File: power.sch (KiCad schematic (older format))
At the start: 37 parts

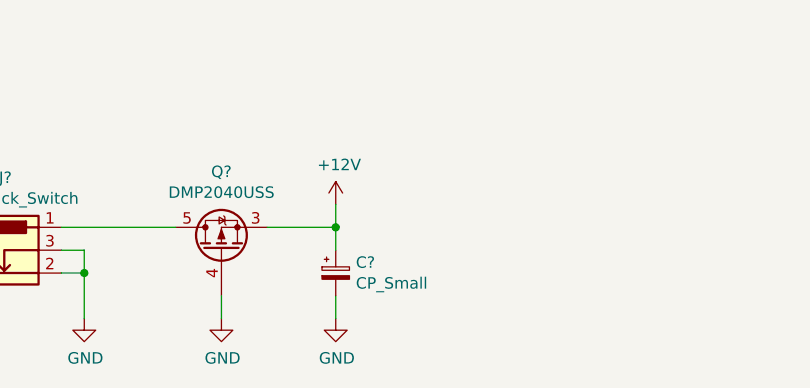
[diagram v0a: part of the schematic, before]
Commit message: sch: Set DC input cap value
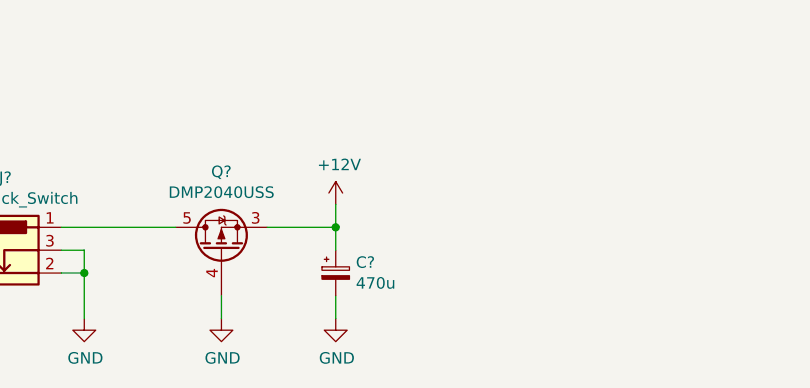
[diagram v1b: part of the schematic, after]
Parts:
- C?: value CP_Small -> 470u
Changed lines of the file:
@@
 P 4200 6900
 F 0 "C?" H 4288 6946 50  0000 L CNN
-F 1 "CP_Small" H 4288 6855 50  0000 L CNN
+F 1 "470u" H 4288 6855 50  0000 L CNN
 F 2 "" H 4200 6900 50  0001 C CNN
 F 3 "~" H 4200 6900 50  0001 C CNN

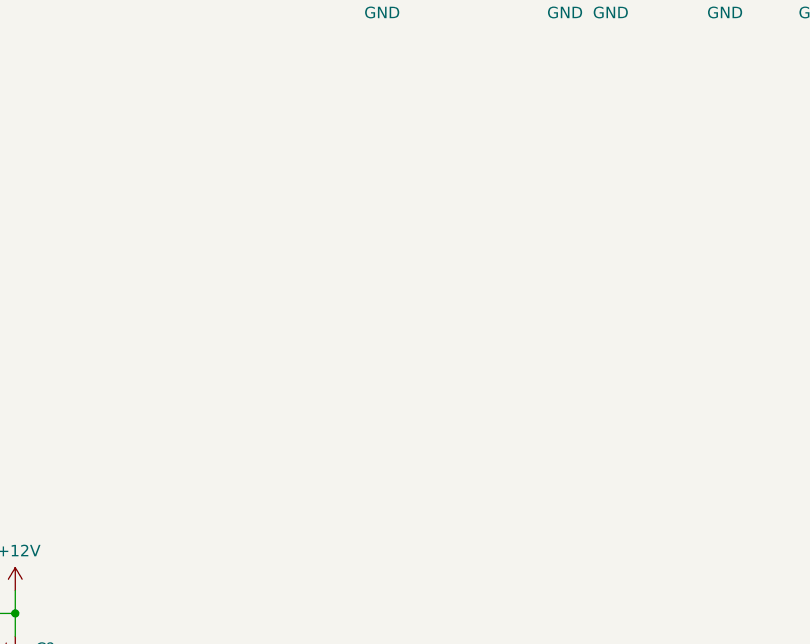
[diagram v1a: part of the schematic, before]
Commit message: sch, lib: Add 1V rail with TPS74401 LDO
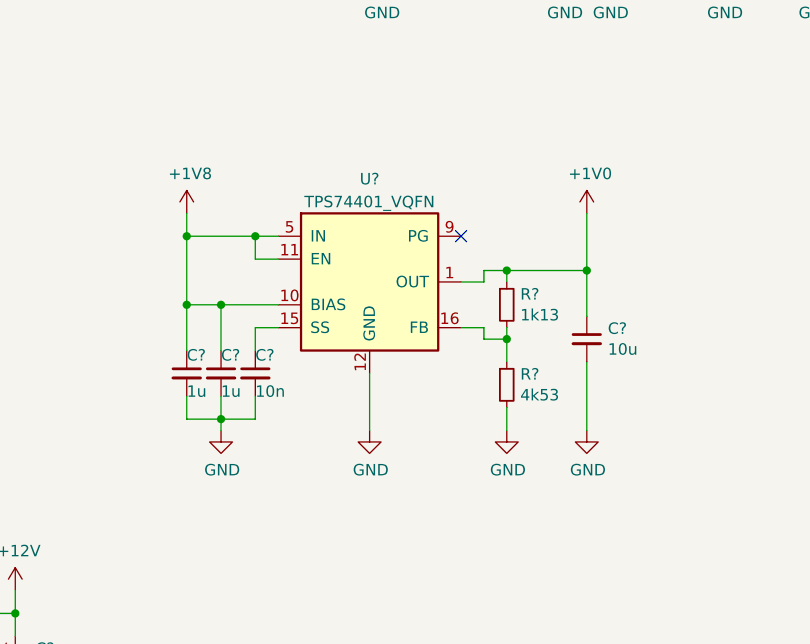
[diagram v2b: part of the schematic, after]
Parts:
- added C?: 10n, symbol Device:C_Small
- added C? (x2): 1u, symbol Device:C_Small
- added C?: 10u, symbol Device:C_Small
- added R?: 1k13, symbol Device:R_Small
- added R?: 4k53, symbol Device:R_Small
- added U?: TPS74401_VQFN, symbol pimouss-motherboard:TPS74401_VQFN
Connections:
- net labels added: +1V0, +1V8
- wire segments 191 -> 224
- no-connect marks 2 -> 3
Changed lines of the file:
@@
 Wire Wire Line
 	4200 7000 4200 7100
+$Comp
+L pimouss-motherboard:TPS74401_VQFN U?
+U 1 1 5CE43F9B
+P 5450 4950
+F 0 "U?" H 5750 5100 50  0000 C CNN
+F 1 "TPS74401_VQFN" H 5750 5000 50  0000 C CNN
+F 2 "" H 6250 4350 50  0001 C CNN
+F 3 "http://www.ti.com/general/docs/lit/getliterature.tsp?genericPartNumber=tps74401&fileType=pdf" H 5450 5450 50  0001 C CNN
+	1    5450 4950
+	1    0    0    -1
+$EndComp
+Wire Wire Line
+	5350 5150 5250 5150
+Wire Wire Line
+	5250 5150 5250 5050
+Wire Wire Line
+	5250 5050 5350 5050
+$Comp
+L Device:C_Small C?
+U 1 1 5CE5AE8A
+P 5250 5650
+F 0 "C?" H 5250 5700 50  0000 L BNN
+F 1 "10n" H 5250 5600 50  0000 L TNN
+F 2 "" H 5250 5650 50  0001 C CNN
+F 3 "~" H 5250 5650 50  0001 C CNN
+	1    5250 5650
+	1    0    0    -1
+$EndComp
+$Comp
+L Device:C_Small C?
+U 1 1 5CE5EC39
+P 5100 5650
+F 0 "C?" H 5100 5700 50  0000 L BNN
+F 1 "1u" H 5100 5600 50  0000 L TNN
+F 2 "" H 5100 5650 50  0001 C CNN
+F 3 "~" H 5100 5650 50  0001 C CNN
+	1    5100 5650
+	1    0    0    -1
+$EndComp
+$Comp
+L Device:C_Small C?
+U 1 1 5CE5F078
+P 4950 5650
+F 0 "C?" H 4950 5700 50  0000 L BNN
+F 1 "1u" H 4950 5600 50  0000 L TNN
+F 2 "" H 4950 5650 50  0001 C CNN
+F 3 "~" H 4950 5650 50  0001 C CNN
+	1    4950 5650
+	1    0    0    -1
+$EndComp
+Wire Wire Line
+	5250 5550 5250 5450
+Wire Wire Line
+	5250 5450 5350 5450
+Wire Wire Line
+	5100 5550 5100 5350
+Wire Wire Line
+	5100 5350 5350 5350
+Wire Wire Line
+	4950 5550 4950 5350
+Wire Wire Line
+	4950 5050 5250 5050
+Connection ~ 5250 5050
+Wire Wire Line
+	4950 5050 4950 4950
+Connection ~ 4950 5050
+$Comp
+L power:+1V8 #PWR?
+U 1 1 5CE8606F
+P 4950 4950
+F 0 "#PWR?" H 4950 4800 50  0001 C CNN
+F 1 "+1V8" H 4965 5123 50  0000 C CNN
+F 2 "" H 4950 4950 50  0001 C CNN
+F 3 "" H 4950 4950 50  0001 C CNN
+	1    4950 4950
+	1    0    0    -1
+$EndComp
+$Comp
+L power:GND #PWR?
+U 1 1 5CE86F6F
+P 5100 5900
+F 0 "#PWR?" H 5100 5650 50  0001 C CNN
+F 1 "GND" H 5105 5727 50  0000 C CNN
+F 2 "" H 5100 5900 50  0001 C CNN
+F 3 "" H 5100 5900 50  0001 C CNN
+	1    5100 5900
+	1    0    0    -1
+$EndComp
+Wire Wire Line
+	4950 5750 4950 5850
+Wire Wire Line
+	4950 5850 5100 5850
+Wire Wire Line
+	5250 5850 5250 5750
+Wire Wire Line
+	5100 5750 5100 5850
+Connection ~ 5100 5850
+Wire Wire Line
+	5100 5850 5250 5850
+Wire Wire Line
+	5100 5850 5100 5900
+$Comp
+L Device:R_Small R?
+U 1 1 5CEBCD64
+P 6350 5350
+F 0 "R?" H 6409 5396 50  0000 L CNN
+F 1 "1k13" H 6409 5305 50  0000 L CNN
+F 2 "" H 6350 5350 50  0001 C CNN
+F 3 "~" H 6350 5350 50  0001 C CNN
+	1    6350 5350
+	1    0    0    -1
+$EndComp
+$Comp
+L Device:R_Small R?
+U 1 1 5CED2DA2
+P 6350 5700
+F 0 "R?" H 6409 5746 50  0000 L CNN
+F 1 "4k53" H 6409 5655 50  0000 L CNN
+F 2 "" H 6350 5700 50  0001 C CNN
+F 3 "~" H 6350 5700 50  0001 C CNN
+	1    6350 5700
+	1    0    0    -1
+$EndComp
+$Comp
+L power:GND #PWR?
+U 1 1 5CED3182
+P 5750 5900
+F 0 "#PWR?" H 5750 5650 50  0001 C CNN
+F 1 "GND" H 5755 5727 50  0000 C CNN
+F 2 "" H 5750 5900 50  0001 C CNN
+F 3 "" H 5750 5900 50  0001 C CNN
+	1    5750 5900
+	1    0    0    -1
+$EndComp
+$Comp
+L power:GND #PWR?
+U 1 1 5CED54E7
+P 6350 5900
+F 0 "#PWR?" H 6350 5650 50  0001 C CNN
+F 1 "GND" H 6355 5727 50  0000 C CNN
+F 2 "" H 6350 5900 50  0001 C CNN
+F 3 "" H 6350 5900 50  0001 C CNN
+	1    6350 5900
+	1    0    0    -1
+$EndComp
+Wire Wire Line
+	6150 5450 6250 5450
+Wire Wire Line
+	6350 5800 6350 5900
+Wire Wire Line
+	5750 5650 5750 5900
+$Comp
+L power:+1V0 #PWR?
+U 1 1 5CF532E8
+P 6700 4950
+F 0 "#PWR?" H 6700 4800 50  0001 C CNN
+F 1 "+1V0" H 6715 5123 50  0000 C CNN
+F 2 "" H 6700 4950 50  0001 C CNN
+F 3 "" H 6700 4950 50  0001 C CNN
+	1    6700 4950
+	1    0    0    -1
+$EndComp
+$Comp
+L Device:C_Small C?
+U 1 1 5CF610D5
+P 6700 5500
+F 0 "C?" H 6792 5546 50  0000 L CNN
+F 1 "10u" H 6792 5455 50  0000 L CNN
+F 2 "" H 6700 5500 50  0001 C CNN
+F 3 "~" H 6700 5500 50  0001 C CNN
+	1    6700 5500
+	1    0    0    -1
+$EndComp
+Wire Wire Line
+	6700 5600 6700 5900
+$Comp
+L power:GND #PWR?
+U 1 1 5CF7AEEC
+P 6700 5900
+F 0 "#PWR?" H 6700 5650 50  0001 C CNN
+F 1 "GND" H 6705 5727 50  0000 C CNN
+F 2 "" H 6700 5900 50  0001 C CNN
+F 3 "" H 6700 5900 50  0001 C CNN
+	1    6700 5900
+	1    0    0    -1
+$EndComp
+Wire Wire Line
+	5100 5350 4950 5350
+Connection ~ 5100 5350
+Connection ~ 4950 5350
+Wire Wire Line
+	4950 5350 4950 5050
+NoConn ~ 6150 5050
+Wire Wire Line
+	6350 5450 6350 5500
+Wire Wire Line
+	6700 4950 6700 5200
+Wire Wire Line
+	6250 5450 6250 5500
+Wire Wire Line
+	6250 5500 6350 5500
+Connection ~ 6350 5500
+Wire Wire Line
+	6350 5500 6350 5600
+Wire Wire Line
+	6150 5250 6250 5250
+Wire Wire Line
+	6250 5250 6250 5200
+Wire Wire Line
+	6250 5200 6350 5200
+Wire Wire Line
+	6350 5200 6350 5250
+Wire Wire Line
+	6350 5200 6700 5200
+Connection ~ 6350 5200
+Connection ~ 6700 5200
+Wire Wire Line
+	6700 5200 6700 5400
 $EndSCHEMATC

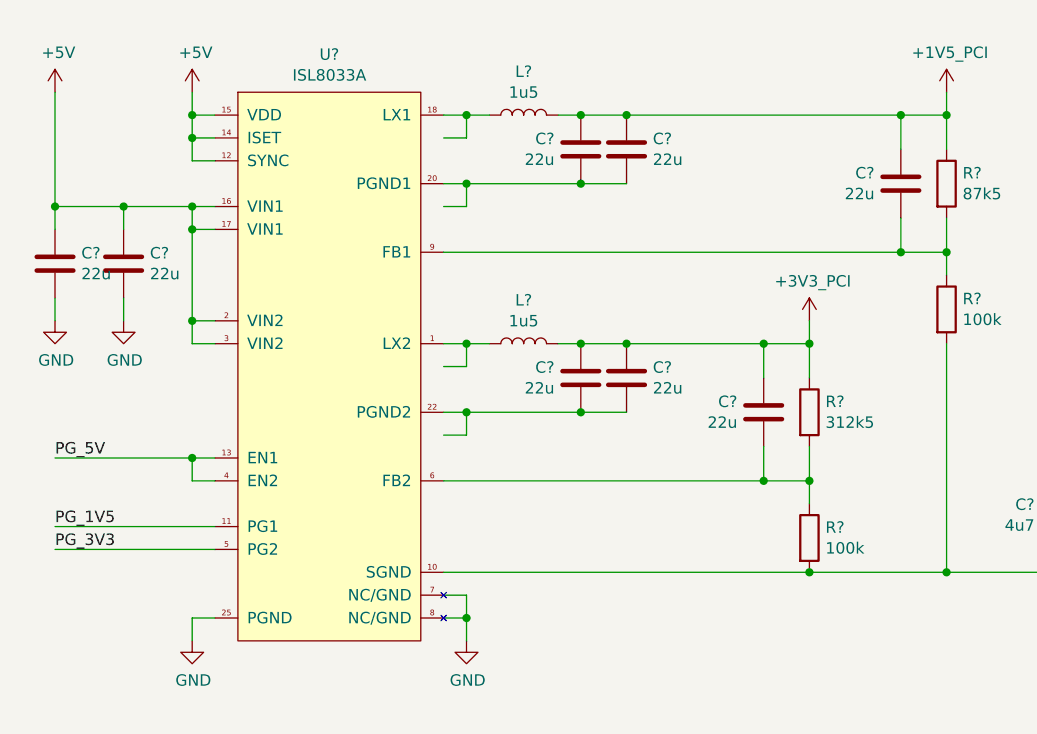
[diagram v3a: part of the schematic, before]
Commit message: sch: Replace regular symbols with small variant
Done for most capacitors and resistors
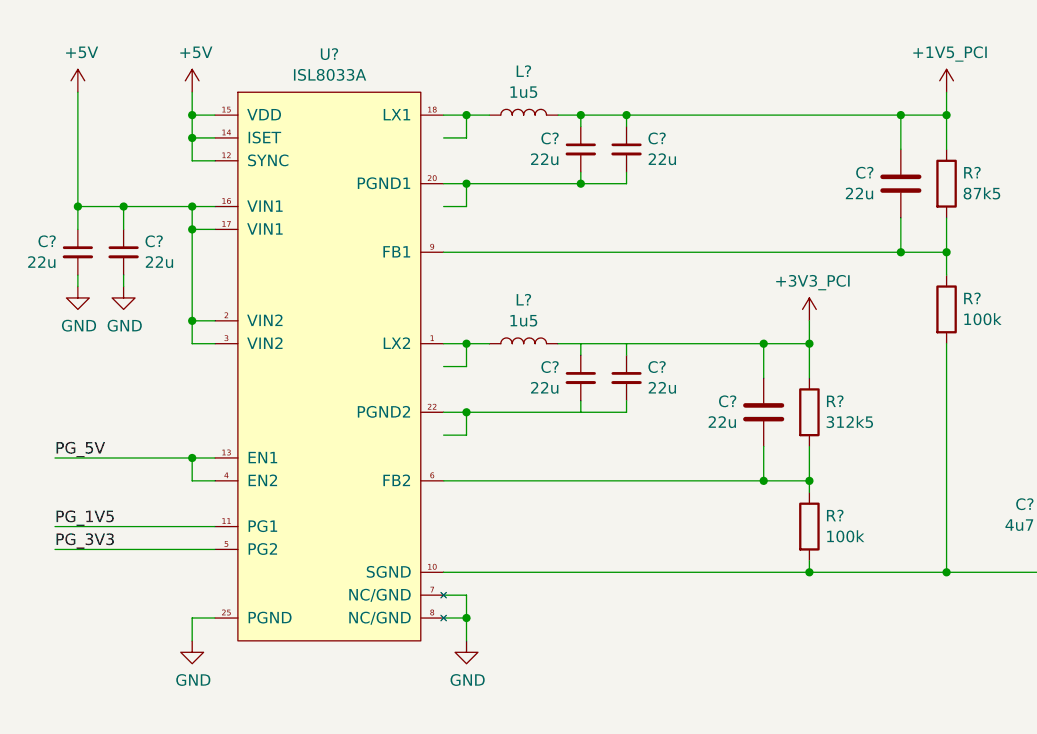
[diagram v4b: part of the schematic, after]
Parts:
- removed C? (x6): 22u, symbol Device:C
- added C? (x6): 22u, symbol Device:C_Small
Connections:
- wire segments 224 -> 230
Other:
- moved on the sheet: R?
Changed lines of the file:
@@
 	1800 2700 1900 2700
 $Comp
-L Device:C C?
-U 1 1 5D0C4B19
-P 1200 2450
-F 0 "C?" H 1315 2496 50  0000 L CNN
-F 1 "22u" H 1315 2405 50  0000 L CNN
-F 2 "" H 1238 2300 50  0001 C CNN
-F 3 "~" H 1200 2450 50  0001 C CNN
-	1    1200 2450
-	1    0    0    -1
-$EndComp
-$Comp
-L Device:C C?
-U 1 1 5D0C4BD2
-P 1500 2450
-F 0 "C?" H 1615 2496 50  0000 L CNN
-F 1 "22u" H 1615 2405 50  0000 L CNN
-F 2 "" H 1538 2300 50  0001 C CNN
-F 3 "~" H 1500 2450 50  0001 C CNN
-	1    1500 2450
-	1    0    0    -1
-$EndComp
-$Comp
 L power:GND #PWR?
 U 1 1 5D0C4D1B
-P 1200 2700
-F 0 "#PWR?" H 1200 2450 50  0001 C CNN
-F 1 "GND" H 1205 2527 50  0000 C CNN
-F 2 "" H 1200 2700 50  0001 C CNN
-F 3 "" H 1200 2700 50  0001 C CNN
-	1    1200 2700
+P 1300 2550
+F 0 "#PWR?" H 1300 2300 50  0001 C CNN
+F 1 "GND" H 1305 2377 50  0000 C CNN
+F 2 "" H 1300 2550 50  0001 C CNN
+F 3 "" H 1300 2550 50  0001 C CNN
+	1    1300 2550
 	1    0    0    -1
 $EndComp
@@
 L power:GND #PWR?
 U 1 1 5D0C4E24
-P 1500 2700
-F 0 "#PWR?" H 1500 2450 50  0001 C CNN
-F 1 "GND" H 1505 2527 50  0000 C CNN
-F 2 "" H 1500 2700 50  0001 C CNN
-F 3 "" H 1500 2700 50  0001 C CNN
-	1    1500 2700
+P 1500 2550
+F 0 "#PWR?" H 1500 2300 50  0001 C CNN
+F 1 "GND" H 1505 2377 50  0000 C CNN
+F 2 "" H 1500 2550 50  0001 C CNN
+F 3 "" H 1500 2550 50  0001 C CNN
+	1    1500 2550
 	1    0    0    -1
 $EndComp
 Connection ~ 1800 2200
 Wire Wire Line
-	1200 2200 1200 1700
-Wire Wire Line
-	1200 2300 1200 2200
-Connection ~ 1200 2200
+	1300 2200 1300 1700
+Wire Wire Line
+	1300 2300 1300 2200
+Connection ~ 1300 2200
 Wire Wire Line
 	1500 2200 1500 2300
 Connection ~ 1500 2200
 Wire Wire Line
-	1500 2200 1200 2200
-Wire Wire Line
-	1500 2600 1500 2700
-Wire Wire Line
-	1200 2600 1200 2700
+	1500 2200 1300 2200
+Wire Wire Line
+	1500 2500 1500 2550
+Wire Wire Line
+	1300 2500 1300 2550
 Wire Wire Line
 	1900 3300 1800 3300
@@
 L power:+5V #PWR?
 U 1 1 5D0C8E77
-P 1200 1700
-F 0 "#PWR?" H 1200 1550 50  0001 C CNN
-F 1 "+5V" H 1215 1873 50  0000 C CNN
-F 2 "" H 1200 1700 50  0001 C CNN
-F 3 "" H 1200 1700 50  0001 C CNN
-	1    1200 1700
+P 1300 1700
+F 0 "#PWR?" H 1300 1550 50  0001 C CNN
+F 1 "+5V" H 1315 1873 50  0000 C CNN
+F 2 "" H 1300 1700 50  0001 C CNN
+F 3 "" H 1300 1700 50  0001 C CNN
+	1    1300 1700
 	1    0    0    -1
 $EndComp
@@
 Wire Wire Line
 	3000 1800 3100 1800
-$Comp
-L Device:C C?
-U 1 1 5D0CC98D
-P 3500 1950
-F 0 "C?" H 3615 1996 50  0000 L CNN
-F 1 "22u" H 3615 1905 50  0000 L CNN
-F 2 "" H 3538 1800 50  0001 C CNN
-F 3 "~" H 3500 1950 50  0001 C CNN
-	1    3500 1950
-	-1   0    0    -1
-$EndComp
-$Comp
-L Device:C C?
-U 1 1 5D0CC9E9
-P 3700 1950
-F 0 "C?" H 3815 1996 50  0000 L CNN
-F 1 "22u" H 3815 1905 50  0000 L CNN
-F 2 "" H 3738 1800 50  0001 C CNN
-F 3 "~" H 3700 1950 50  0001 C CNN
-	1    3700 1950
-	1    0    0    -1
-$EndComp
 Wire Wire Line
 	2900 2100 3000 2100
@@
 Wire Wire Line
 	4900 2400 5100 2400
-Wire Wire Line
-	3400 1800 3500 1800
-Connection ~ 3500 1800
-Wire Wire Line
-	3500 1800 3700 1800
-Connection ~ 3700 1800
-Wire Wire Line
-	3700 1800 4900 1800
-Wire Wire Line
-	3000 2100 3500 2100
 Connection ~ 3000 2100
-Wire Wire Line
-	3500 2100 3700 2100
-Connection ~ 3500 2100
 Wire Wire Line
 	2900 2400 4900 2400
@@
 Wire Wire Line
 	3000 2800 3100 2800
-$Comp
-L Device:C C?
-U 1 1 5D0F0745
-P 3500 2950
-F 0 "C?" H 3615 2996 50  0000 L CNN
-F 1 "22u" H 3615 2905 50  0000 L CNN
-F 2 "" H 3538 2800 50  0001 C CNN
-F 3 "~" H 3500 2950 50  0001 C CNN
-	1    3500 2950
-	-1   0    0    -1
-$EndComp
-$Comp
-L Device:C C?
-U 1 1 5D0F074C
-P 3700 2950
-F 0 "C?" H 3815 2996 50  0000 L CNN
-F 1 "22u" H 3815 2905 50  0000 L CNN
-F 2 "" H 3738 2800 50  0001 C CNN
-F 3 "~" H 3700 2950 50  0001 C CNN
-	1    3700 2950
-	1    0    0    -1
-$EndComp
 Wire Wire Line
 	2900 3100 3000 3100
@@
 L Device:R R?
 U 1 1 5D0F0760
-P 4500 3650
-F 0 "R?" H 4570 3696 50  0000 L CNN
-F 1 "100k" H 4570 3605 50  0000 L CNN
-F 2 "" V 4430 3650 50  0001 C CNN
-F 3 "~" H 4500 3650 50  0001 C CNN
-	1    4500 3650
+P 4500 3600
+F 0 "R?" H 4570 3646 50  0000 L CNN
+F 1 "100k" H 4570 3555 50  0000 L CNN
+F 2 "" V 4430 3600 50  0001 C CNN
+F 3 "~" H 4500 3600 50  0001 C CNN
+	1    4500 3600
 	1    0    0    -1
 $EndComp
@@
 Wire Wire Line
 	4300 3400 4500 3400
-Wire Wire Line
-	3400 2800 3500 2800
-Connection ~ 3500 2800
-Wire Wire Line
-	3500 2800 3700 2800
-Connection ~ 3700 2800
-Wire Wire Line
-	3700 2800 4300 2800
-Wire Wire Line
-	3000 3100 3500 3100
 Connection ~ 3000 3100
 Wire Wire Line
-	3500 3100 3700 3100
-Connection ~ 3500 3100
-Wire Wire Line
 	2900 3400 4300 3400
 Wire Wire Line
-	4500 3400 4500 3500
-Connection ~ 4500 3400
-Wire Wire Line
-	2900 3800 4500 3800
-Wire Wire Line
-	4500 3800 5100 3800
-Wire Wire Line
 	5100 3800 5100 2800
-Connection ~ 4500 3800
 $Comp
 L pimouss-motherboard:+1V5_PCI #PWR?
@@
 Wire Wire Line
 	6700 5200 6700 5400
+$Comp
+L Device:C_Small C?
+U 1 1 5D669FE3
+P 3700 1950
+F 0 "C?" H 3792 1996 50  0000 L CNN
+F 1 "22u" H 3792 1905 50  0000 L CNN
+F 2 "" H 3700 1950 50  0001 C CNN
+F 3 "~" H 3700 1950 50  0001 C CNN
+	1    3700 1950
+	1    0    0    -1
+$EndComp
+Wire Wire Line
+	3000 2100 3500 2100
+$Comp
+L Device:C_Small C?
+U 1 1 5D682EA3
+P 3500 1950
+F 0 "C?" H 3408 1996 50  0000 R CNN
+F 1 "22u" H 3408 1905 50  0000 R CNN
+F 2 "" H 3500 1950 50  0001 C CNN
+F 3 "~" H 3500 1950 50  0001 C CNN
+	1    3500 1950
+	1    0    0    -1
+$EndComp
+Wire Wire Line
+	3400 1800 3500 1800
+Wire Wire Line
+	3500 1850 3500 1800
+Connection ~ 3500 1800
+Wire Wire Line
+	3500 1800 3700 1800
+Wire Wire Line
+	3700 1850 3700 1800
+Connection ~ 3700 1800
+Wire Wire Line
+	3700 1800 4900 1800
+Wire Wire Line
+	3500 2050 3500 2100
+Connection ~ 3500 2100
+Wire Wire Line
+	3500 2100 3700 2100
+Wire Wire Line
+	3700 2050 3700 2100
+Wire Wire Line
+	3000 3100 3700 3100
+Wire Wire Line
+	3400 2800 4300 2800
+$Comp
+L Device:C_Small C?
+U 1 1 5D6C30F8
+P 3700 2950
+F 0 "C?" H 3792 2996 50  0000 L CNN
+F 1 "22u" H 3792 2905 50  0000 L CNN
+F 2 "" H 3700 2950 50  0001 C CNN
+F 3 "~" H 3700 2950 50  0001 C CNN
+	1    3700 2950
+	1    0    0    -1
+$EndComp
+$Comp
+L Device:C_Small C?
+U 1 1 5D6C30FE
+P 3500 2950
+F 0 "C?" H 3408 2996 50  0000 R CNN
+F 1 "22u" H 3408 2905 50  0000 R CNN
+F 2 "" H 3500 2950 50  0001 C CNN
+F 3 "~" H 3500 2950 50  0001 C CNN
+	1    3500 2950
+	1    0    0    -1
+$EndComp
+Wire Wire Line
+	3500 2850 3500 2800
+Wire Wire Line
+	3700 2850 3700 2800
+Wire Wire Line
+	3500 3050 3500 3100
+Wire Wire Line
+	3700 3050 3700 3100
+$Comp
+L Device:C_Small C?
+U 1 1 5D6DF150
+P 1500 2400
+F 0 "C?" H 1592 2446 50  0000 L CNN
+F 1 "22u" H 1592 2355 50  0000 L CNN
+F 2 "" H 1500 2400 50  0001 C CNN
+F 3 "~" H 1500 2400 50  0001 C CNN
+	1    1500 2400
+	1    0    0    -1
+$EndComp
+$Comp
+L Device:C_Small C?
+U 1 1 5D6DF156
+P 1300 2400
+F 0 "C?" H 1208 2446 50  0000 R CNN
+F 1 "22u" H 1208 2355 50  0000 R CNN
+F 2 "" H 1300 2400 50  0001 C CNN
+F 3 "~" H 1300 2400 50  0001 C CNN
+	1    1300 2400
+	1    0    0    -1
+$EndComp
+Wire Wire Line
+	2900 3800 4500 3800
+Wire Wire Line
+	4500 3400 4500 3450
+Connection ~ 4500 3400
+Wire Wire Line
+	4500 3750 4500 3800
+Connection ~ 4500 3800
+Wire Wire Line
+	4500 3800 5100 3800
 $EndSCHEMATC

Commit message: sch: Misc fixes
- add missing NC on PCIe switch
- fix incorrect cap values on PCIe supply
- fix main schematic interco labels
- fix PHY JTAG signal name
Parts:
- C? (x2): value 22u -> 12p
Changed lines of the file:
@@
 P 4900 2100
 F 0 "C?" H 5015 2146 50  0000 L CNN
-F 1 "22u" H 5015 2055 50  0000 L CNN
+F 1 "12p" H 5015 2055 50  0000 L CNN
 F 2 "" H 4938 1950 50  0001 C CNN
 F 3 "~" H 4900 2100 50  0001 C CNN
@@
 P 4300 3100
 F 0 "C?" H 4415 3146 50  0000 L CNN
-F 1 "22u" H 4415 3055 50  0000 L CNN
+F 1 "12p" H 4415 3055 50  0000 L CNN
 F 2 "" H 4338 2950 50  0001 C CNN
 F 3 "~" H 4300 3100 50  0001 C CNN
